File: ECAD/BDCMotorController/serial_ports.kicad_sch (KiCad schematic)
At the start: 9 parts, among them J5 DE9_Pins_MountingHoles, J6 DE9_Pins_MountingHoles, J7 DE9_Pins_MountingHoles, U31 PCA9555PW, U32 PCA9555PW

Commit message: Progress ECAD.
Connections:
- net DCD_IN1: now also U31.4 (IO0_0); no longer U31.11 (IO0_7)
- net DTR_IN1: now also U31.11 (IO0_7); no longer U31.8 (IO0_4)
- net RI_IN1: now also U31.5 (IO0_1); no longer U31.9 (IO0_5)
- net RTS_IN1: now also U31.10 (IO0_6); no longer U31.5 (IO0_1)
- net ST_IN1: now also U31.8 (IO0_4); no longer U31.4 (IO0_0)
- net ~{SHDN_IN1}: now also U31.9 (IO0_5); no longer U31.10 (IO0_6)
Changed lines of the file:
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@@
 	)
 	(label "ST_IN1"
-		(at 100.33 35.56 180)
+		(at 100.33 45.72 180)
 		(effects
 			(font
@@
 	)
 	(label "DCD_IN1"
-		(at 100.33 53.34 180)
+		(at 100.33 35.56 180)
 		(effects
 			(font
@@
 	)
 	(label "RTS_IN1"
-		(at 100.33 38.1 180)
+		(at 100.33 50.8 180)
 		(effects
 			(font
@@
 	)
 	(label "RI_IN1"
-		(at 100.33 48.26 180)
+		(at 100.33 38.1 180)
 		(effects
 			(font
@@
 	)
 	(label "DTR_IN1"
-		(at 100.33 45.72 180)
+		(at 100.33 53.34 180)
 		(effects
 			(font
@@
 	)
 	(label "~{SHDN_IN1}"
-		(at 100.33 50.8 180)
-		(effects
-			(font
+		(at 100.33 48.26 180)
+		(effects
+			(font

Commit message: Progressed ECAD.
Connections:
- net CTS_IN2: now also U31.18 (IO1_5); no longer U31.17 (IO1_4)
- net CTS_IN3: now also U32.18 (IO1_5); no longer U32.7 (IO0_3)
- net DCD_IN3: now also U32.15 (IO1_2); no longer U32.11 (IO0_7)
- net DSR_IN2: now also U31.17 (IO1_4); no longer U31.18 (IO1_5)
- net DSR_IN3: now also U32.17 (IO1_4); no longer U32.6 (IO0_2)
- net DTR_IN2: now also U31.14 (IO1_1); no longer U31.16 (IO1_3)
- net DTR_IN3: now also U32.14 (IO1_1); no longer U32.8 (IO0_4)
- net RI_IN2: now also U31.16 (IO1_3); no longer U31.13 (IO1_0)
- net RI_IN3: now also U32.16 (IO1_3); no longer U32.9 (IO0_5)
- net RTS_IN2: now also U31.13 (IO1_0); no longer U31.20 (IO1_7)
- net RTS_IN3: now also U32.13 (IO1_0); no longer U32.5 (IO0_1)
- net ST_IN3: now also U32.19 (IO1_6); no longer U32.4 (IO0_0)
- net ~{SHDN_IN2}: now also U31.20 (IO1_7); no longer U31.14 (IO1_1)
- net ~{SHDN_IN3}: now also U32.20 (IO1_7); no longer U32.10 (IO0_6)
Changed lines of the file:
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@@
 	)
 	(no_connect
-		(at 90.17 142.24)
+		(at 90.17 104.14)
 	)
 	(no_connect
-		(at 90.17 137.16)
+		(at 90.17 106.68)
 	)
 	(no_connect
-		(at 90.17 139.7)
+		(at 90.17 111.76)
 	)
 	(no_connect
-		(at 90.17 132.08)
+		(at 90.17 114.3)
 	)
 	(no_connect
-		(at 90.17 134.62)
+		(at 90.17 109.22)
 	)
 	(no_connect
-		(at 90.17 144.78)
+		(at 90.17 119.38)
 	)
 	(no_connect
-		(at 90.17 129.54)
+		(at 90.17 116.84)
 	)
 	(no_connect
-		(at 90.17 127)
+		(at 90.17 121.92)
 	)
 	(wire
@@
 	(wire
 		(pts
-			(xy 90.17 121.92) (xy 100.33 121.92)
+			(xy 90.17 132.08) (xy 100.33 132.08)
 		)
 		(stroke
@@
 	(wire
 		(pts
-			(xy 90.17 116.84) (xy 100.33 116.84)
+			(xy 90.17 134.62) (xy 100.33 134.62)
 		)
 		(stroke
@@
 	(wire
 		(pts
-			(xy 90.17 109.22) (xy 100.33 109.22)
+			(xy 90.17 137.16) (xy 100.33 137.16)
 		)
 		(stroke
@@
 	(wire
 		(pts
-			(xy 90.17 106.68) (xy 100.33 106.68)
+			(xy 90.17 127) (xy 100.33 127)
 		)
 		(stroke
@@
 	(wire
 		(pts
-			(xy 90.17 111.76) (xy 100.33 111.76)
+			(xy 90.17 139.7) (xy 100.33 139.7)
 		)
 		(stroke
@@
 	(wire
 		(pts
-			(xy 90.17 119.38) (xy 100.33 119.38)
+			(xy 90.17 144.78) (xy 100.33 144.78)
 		)
 		(stroke
@@
 	(wire
 		(pts
-			(xy 90.17 114.3) (xy 100.33 114.3)
+			(xy 90.17 129.54) (xy 100.33 129.54)
 		)
 		(stroke
@@
 	(wire
 		(pts
-			(xy 90.17 104.14) (xy 100.33 104.14)
+			(xy 90.17 142.24) (xy 100.33 142.24)
 		)
 		(stroke
@@
 	)
 	(label "RTS_IN2"
-		(at 100.33 76.2 180)
+		(at 100.33 58.42 180)
 		(effects
 			(font
@@
 	)
 	(label "DTR_IN3"
-		(at 100.33 114.3 180)
+		(at 100.33 129.54 180)
 		(effects
 			(font
@@
 	)
 	(label "CTS_IN3"
-		(at 100.33 111.76 180)
+		(at 100.33 139.7 180)
 		(effects
 			(font
@@
 	)
 	(label "DTR_IN2"
-		(at 100.33 66.04 180)
+		(at 100.33 60.96 180)
 		(effects
 			(font
@@
 	)
 	(label "ST_IN3"
-		(at 100.33 104.14 180)
+		(at 100.33 142.24 180)
 		(effects
 			(font
@@
 	)
 	(label "CTS_IN2"
-		(at 100.33 68.58 180)
+		(at 100.33 71.12 180)
 		(effects
 			(font
@@
 	)
 	(label "DSR_IN2"
-		(at 100.33 71.12 180)
+		(at 100.33 68.58 180)
 		(effects
 			(font
@@
 	)
 	(label "DSR_IN3"
-		(at 100.33 109.22 180)
+		(at 100.33 137.16 180)
 		(effects
 			(font
@@
 	)
 	(label "RTS_IN3"
-		(at 100.33 106.68 180)
+		(at 100.33 127 180)
 		(effects
 			(font
@@
 	)
 	(label "RI_IN3"
-		(at 100.33 116.84 180)
+		(at 100.33 134.62 180)
 		(effects
 			(font
@@
 	)
 	(label "~{SHDN_IN3}"
-		(at 100.33 119.38 180)
+		(at 100.33 144.78 180)
 		(effects
 			(font
@@
 	)
 	(label "RI_IN2"
-		(at 100.33 58.42 180)
+		(at 100.33 66.04 180)
 		(effects
 			(font
@@
 	)
 	(label "DCD_IN3"
-		(at 100.33 121.92 180)
+		(at 100.33 132.08 180)
 		(effects
 			(font
@@
 	)
 	(label "~{SHDN_IN2}"
-		(at 100.33 60.96 180)
-		(effects
-			(font
+		(at 100.33 76.2 180)
+		(effects
+			(font

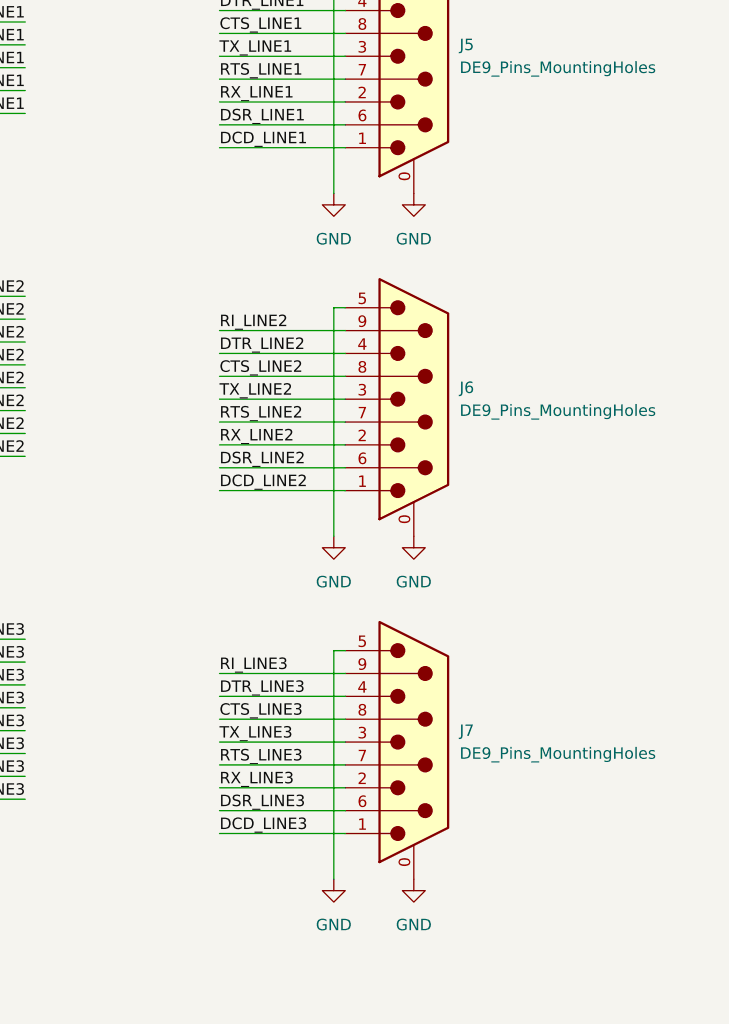
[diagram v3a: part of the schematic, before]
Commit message: Updated schematic from kicad version 9.0 to 10.0.
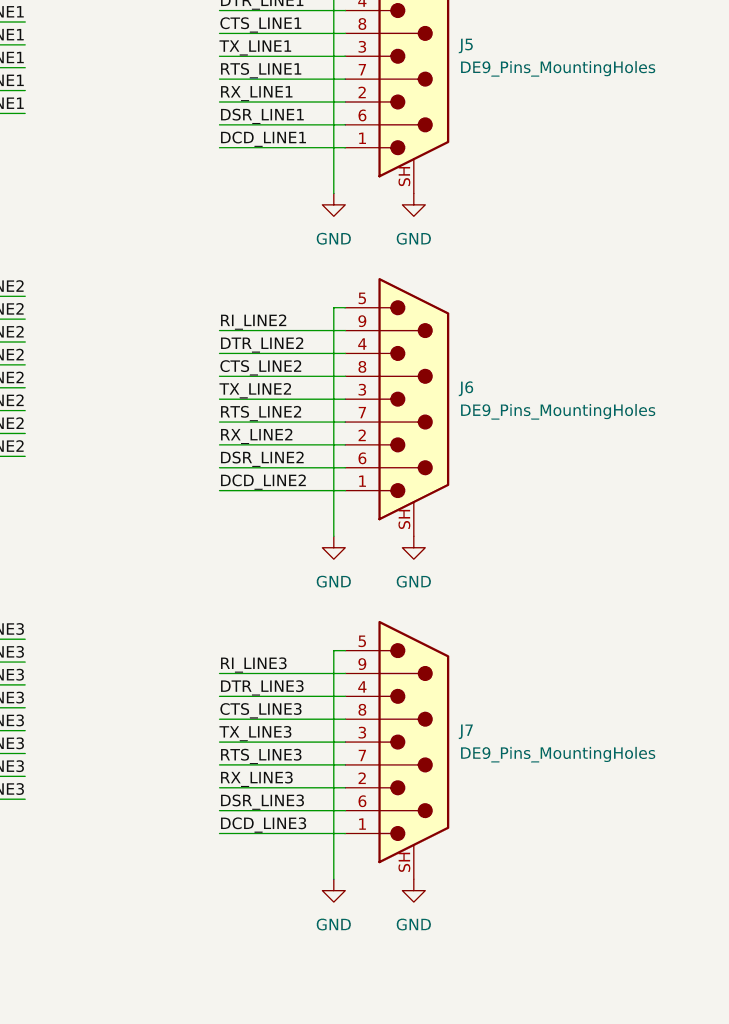
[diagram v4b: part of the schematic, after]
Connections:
- net GND: now also J5.SH (PAD), J6.SH (PAD), J7.SH (PAD); no longer J5.0 (PAD), J6.0 (PAD), J7.0 (PAD)

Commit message: Progressed ECAD.
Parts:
- U31, U32: Status OK -> (none)
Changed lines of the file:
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@@
 			)
 		)
-		(property "Status" "OK"
+		(property "Status" ""
 			(at 77.47 55.88 0)
 			(hide yes)
@@
 			)
 		)
-		(property "Status" "OK"
+		(property "Status" ""
 			(at 77.47 124.46 0)
 			(hide yes)

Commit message: Progressed ECAD.
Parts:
- U31, U32: Status (none) -> OK
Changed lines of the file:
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@@
 			)
 		)
-		(property "Status" ""
+		(property "Status" "OK"
 			(at 77.47 55.88 0)
 			(hide yes)
@@
 			)
 		)
-		(property "Status" ""
+		(property "Status" "OK"
 			(at 77.47 124.46 0)
 			(hide yes)

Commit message: Progressed ECAD.
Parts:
- J5, J6, J7: MPN (none) -> 2301826-2; Status (none) -> OK
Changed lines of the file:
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@@
 			)
 		)
-		(property "Datasheet" ""
+		(property "Datasheet" "https://www.lcsc.com/datasheet/C3099734.pdf"
 			(at 233.68 88.9 0)
 			(hide yes)
@@
 		)
 		(property "Sim.Type" ""
+			(at 233.68 88.9 0)
+			(hide yes)
+			(show_name no)
+			(do_not_autoplace no)
+			(effects
+				(font
+					(size 1.27 1.27)
+				)
+			)
+		)
+		(property "MPN" "2301826-2"
+			(at 233.68 88.9 0)
+			(hide yes)
+			(show_name no)
+			(do_not_autoplace no)
+			(effects
+				(font
+					(size 1.27 1.27)
+				)
+			)
+		)
+		(property "Status" "OK"
 			(at 233.68 88.9 0)
 			(hide yes)
@@
 			)
 		)
-		(property "Datasheet" ""
+		(property "Datasheet" "https://www.lcsc.com/datasheet/C3099734.pdf"
 			(at 233.68 50.8 0)
 			(hide yes)
@@
 		)
 		(property "Sim.Type" ""
+			(at 233.68 50.8 0)
+			(hide yes)
+			(show_name no)
+			(do_not_autoplace no)
+			(effects
+				(font
+					(size 1.27 1.27)
+				)
+			)
+		)
+		(property "MPN" "2301826-2"
+			(at 233.68 50.8 0)
+			(hide yes)
+			(show_name no)
+			(do_not_autoplace no)
+			(effects
+				(font
+					(size 1.27 1.27)
+				)
+			)
+		)
+		(property "Status" "OK"
 			(at 233.68 50.8 0)
 			(hide yes)
@@
 			)
 		)
-		(property "Datasheet" ""
+		(property "Datasheet" "https://www.lcsc.com/datasheet/C3099734.pdf"
 			(at 233.68 127 0)
 			(hide yes)
@@
 			(at 233.68 127 0)
 			(hide yes)
+			(show_name no)
+			(do_not_autoplace no)
+			(effects
+				(font
+					(size 1.27 1.27)
+				)
+			)
+		)
+		(property "MPN" "2301826-2"
+			(at 233.68 127 0)
+			(hide yes)
+			(show_name no)
+			(do_not_autoplace no)
+			(effects
+				(font
+					(size 1.27 1.27)
+				)
+			)
+		)
+		(property "Status" "OK"
+			(at 233.68 127 0)
+			(hide yes)
